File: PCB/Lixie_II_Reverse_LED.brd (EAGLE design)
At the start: 47.5 x 45 mm, 48 parts

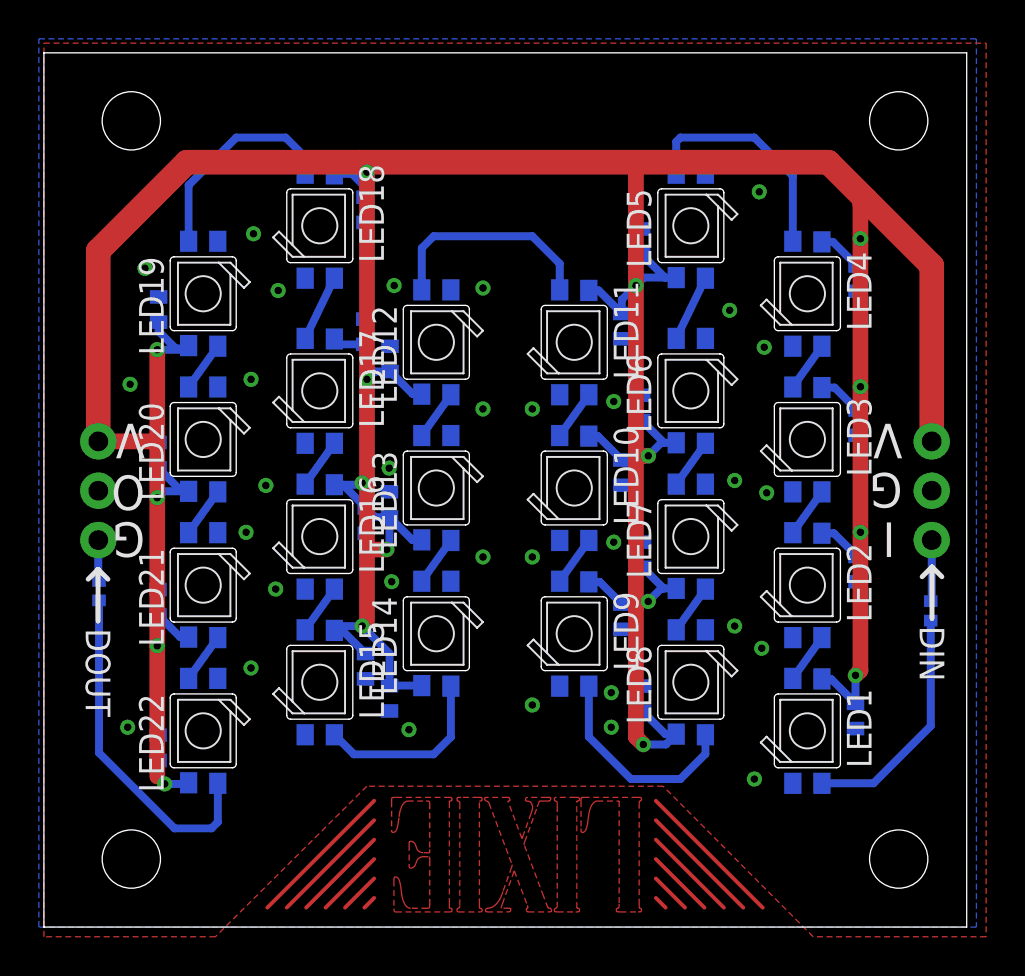
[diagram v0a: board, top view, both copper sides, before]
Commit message: Adjusted light filter and base alignments
Fixes issues #1 #2 #3
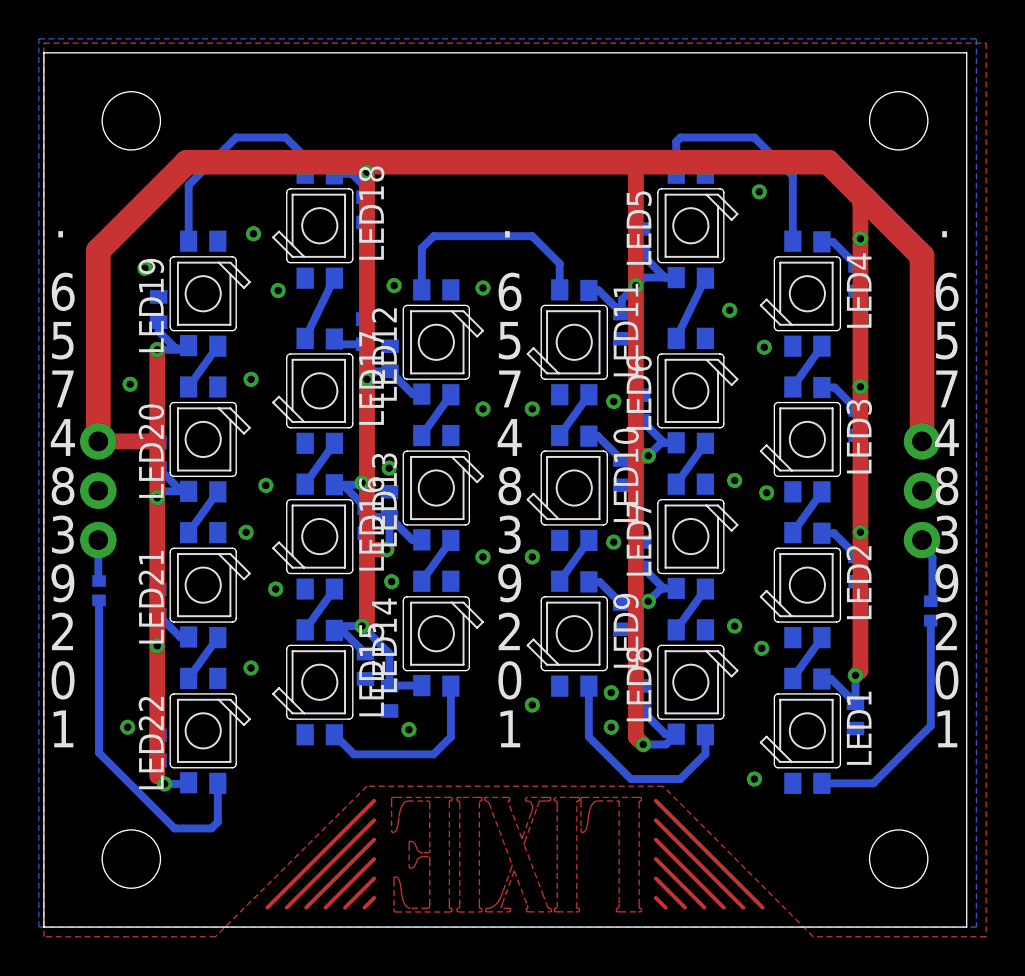
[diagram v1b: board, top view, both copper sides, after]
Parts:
- moved J1 0.50 mm to (45.5, 25.0)
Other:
- board text added: "."
- board text added: "0"
- board text added: "1"
- board text added: "2"
- board text added: "3"
- board text added: "4"
- board text added: "5"
- board text added: "6"
- board text added: "7"
- board text added: "8"
- board text added: "9"
- board text added: "LIXIE II CLONE REV.1.2"
- board text removed: "DIN"
- board text removed: "DOUT"
- board text removed: "LIXIE II CLONE REV.1.1"
